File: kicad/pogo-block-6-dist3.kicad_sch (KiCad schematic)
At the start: 62 parts, among them U33 CD4053, U38 TL072, U39 TL072, U44 TL072, U45 TL072, U77 CD4053

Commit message: 0018: block-6 stage 2 - distortion BEFORE bandpass (0017 reorder)
The core 0017 change: flip the per-band order from SVF->DIST to DIST->SVF to
match the plugin (Pogo.cpp:443-451). Realized as a net re-point across the 7
split sections (no part changes):
  LP1_OUT / BP3IN  ->  distN (R18/R20/R22 distortion inputs)
                   ->  mux out (BPn_DISTOUT)  ->  svfN SUM_AMP (R13)
                   ->  SVF v1 buffer (BPn_BANDOUT / BP3_TAP)  ->  mix wet summer
- BP1/BP2 take the LP1 band; BP3 takes BP3IN (the ALT/LP1 selector, stage 3).
- BP3 OUT tap now taken post-bandpass (BP3_TAP = svf3 v1), matching the plugin
  (prevOut[2]); block-B keeps the BP3_TAP net name (no block-B change).
- spec §1/§2 updated: signal order, DIST knob, ALT path (through-VCA/BP3-only),
  BP3 tap point.

Boundary symmetry verified for all re-pointed nets; all 5 --check gates +
parity green.

https://claude.ai/code/session_013jFXG5oeMVSYP7iRpwGvtQ
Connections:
- net BP3_BPBUF_L renamed BP3IN_L
- net BP3_BPBUF_R renamed BP3IN_R
- net BP3_TAP_L renamed BP3_DISTOUT_L
- net BP3_TAP_R renamed BP3_DISTOUT_R
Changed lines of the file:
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@@
   (effects (font (size 1.016 1.016)) (justify left))
 )
-(global_label "BP3_BPBUF_L"
+(global_label "BP3IN_L"
   (shape output)
   (at 40.000 373.810 0)
   (effects (font (size 1.016 1.016)) (justify left))
 )
-(global_label "BP3_BPBUF_L"
+(global_label "BP3IN_L"
   (shape output)
   (at 160.000 373.810 0)
   (effects (font (size 1.016 1.016)) (justify left))
 )
-(global_label "BP3_BPBUF_L"
+(global_label "BP3IN_L"
   (shape output)
   (at 100.000 428.810 0)
   (effects (font (size 1.016 1.016)) (justify left))
 )
-(global_label "BP3_BPBUF_L"
+(global_label "BP3IN_L"
   (shape output)
   (at 40.000 538.810 0)
   (effects (font (size 1.016 1.016)) (justify left))
 )
-(global_label "BP3_BPBUF_L"
+(global_label "BP3IN_L"
   (shape output)
   (at 100.000 538.810 0)
   (effects (font (size 1.016 1.016)) (justify left))
 )
-(global_label "BP3_BPBUF_R"
+(global_label "BP3IN_R"
   (shape output)
   (at 40.000 758.810 0)
   (effects (font (size 1.016 1.016)) (justify left))
 )
-(global_label "BP3_BPBUF_R"
+(global_label "BP3IN_R"
   (shape output)
   (at 160.000 758.810 0)
   (effects (font (size 1.016 1.016)) (justify left))
 )
-(global_label "BP3_BPBUF_R"
+(global_label "BP3IN_R"
   (shape output)
   (at 100.000 813.810 0)
   (effects (font (size 1.016 1.016)) (justify left))
 )
-(global_label "BP3_BPBUF_R"
+(global_label "BP3IN_R"
   (shape output)
   (at 40.000 923.810 0)
   (effects (font (size 1.016 1.016)) (justify left))
 )
-(global_label "BP3_BPBUF_R"
+(global_label "BP3IN_R"
   (shape output)
   (at 100.000 923.810 0)
@@
   (effects (font (size 1.016 1.016)) (justify left))
 )
-(global_label "BP3_TAP_L"
+(global_label "BP3_DISTOUT_L"
   (shape output)
   (at 48.890 50.160 0)
   (effects (font (size 1.016 1.016)) (justify left))
 )
-(global_label "BP3_TAP_R"
+(global_label "BP3_DISTOUT_R"
   (shape output)
   (at 48.890 42.540 0)

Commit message: 0018: block-6 stage 3 - BP3 input selector (ALT-VCA vs LP1)
Build the BP3 input selector the plugin requires (Pogo.cpp:440-441): a CD4053
mux (U81, block-6-dist3) picks per channel between the LP1 band (LP1_OUT) and
the ALT-VCA voice (block-4 ALT_VCA_OUT), feeding BP3's distortion input.
- Select = ALT_L_DET, an ALT_BP_L insertion detect: J3 tip-switch lug (block-1)
  -> ALT_L_DET, +12V pull-up (R133, dist3) + 22k tip pulldown (R134, block-1);
  patched=ALT-VCA, unpatched=LP1.
- BP3IN is now an internal dist3 net (mux out -> distortion), resolving the
  previously hand-waved boundary. New boundary nets: ALT_L_DET (block-1->dist3),
  ALT_VCA_OUT_L/R (block-4->dist3), LP1_OUT extended to dist3.
- Single ALT_L_DET drives both channels (user decision): the locked single-switch
  jacks leave no free contact for an ALT_R detect (J4's switch is the R-normal),
  so the plugin's asymmetric bp3InR=(L||R) is dropped -- diverges only in the
  rare R-patched-not-L case.

CD4053 selector + components (G5/G6a). All 5 --check gates + parity green;
boundary symmetry verified.

https://claude.ai/code/session_013jFXG5oeMVSYP7iRpwGvtQ
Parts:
- added C110_U81n, C110_U81p: 100nF, symbol Device:C
- added R133: 100k, symbol Device:R
- added U81: CD4053, POGO_Package_SO:SOIC-16_3.9x9.9mm_P1.27mm, symbol Analog_Switch:CD4053
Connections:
- net +12V: now also C110_U81p.2, R133.2, U81.9 (C)
- net -12V: now also C110_U81n.2, U81.11 (A)
- net BP3IN_L: now also U81.5 (Z0)
- net BP3IN_R: now also U81.2 (Y0)
- net GND: now also C110_U81n.1, C110_U81p.1, U81.10 (B), U81.12 (X0), U81.13 (X1), U81.14 (X), U81.16 (VDD), U81.6 (INH)
- new net ALT_L_DET: R133.1, U81.7 (VEE), U81.8 (VSS)
- new net ALT_VCA_OUT_L: U81.3 (Z1)
- new net ALT_VCA_OUT_R: U81.1 (Y1)
- new net LP1_OUT_L: U81.4 (Z)
- new net LP1_OUT_R: U81.15 (Y)
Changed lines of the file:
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@@
     (effects (font (size 1.016 1.016)) (justify left) (hide yes)))
 )
+(symbol
+  (lib_id "Analog_Switch:CD4053")
+  (at 160.000 1140.000 0)
+  (unit 1)
+  (in_bom yes)
+  (on_board yes)
+  (property "Reference" "U81" (at 163.000 1143.000 0)
+    (effects (font (size 1.27 1.27)) (justify left)))
+  (property "Value" "CD4053" (at 163.000 1139.500 0)
+    (effects (font (size 1.016 1.016)) (justify left) (hide yes)))
+  (property "Footprint" "POGO_Package_SO:SOIC-16_3.9x9.9mm_P1.27mm" (at 160.000 1140.000 0)
+    (effects (font (size 1.016 1.016)) (hide yes)))
+)
+(symbol
+  (lib_id "Device:C")
+  (at 40.000 1195.000 0)
+  (unit 1)
+  (in_bom yes)
+  (on_board yes)
+  (property "Reference" "C110_U81p" (at 43.000 1198.000 0)
+    (effects (font (size 1.27 1.27)) (justify left)))
+  (property "Value" "100nF" (at 43.000 1194.500 0)
+    (effects (font (size 1.016 1.016)) (justify left) (hide yes)))
+)
+(symbol
+  (lib_id "Device:C")
+  (at 100.000 1195.000 0)
+  (unit 1)
+  (in_bom yes)
+  (on_board yes)
+  (property "Reference" "C110_U81n" (at 103.000 1198.000 0)
+    (effects (font (size 1.27 1.27)) (justify left)))
+  (property "Value" "100nF" (at 103.000 1194.500 0)
+    (effects (font (size 1.016 1.016)) (justify left) (hide yes)))
+)
+(symbol
+  (lib_id "Device:R")
+  (at 160.000 1195.000 0)
+  (unit 1)
+  (in_bom yes)
+  (on_board yes)
+  (property "Reference" "R133" (at 163.000 1198.000 0)
+    (effects (font (size 1.27 1.27)) (justify left)))
+  (property "Value" "100k" (at 163.000 1194.500 0)
+    (effects (font (size 1.016 1.016)) (justify left) (hide yes)))
+)
 (global_label "V5LOGIC"
   (shape output)
@@
 )
 (global_label "BP3IN_L"
-  (shape output)
+  (shape input)
+  (at 168.890 1150.160 0)
+  (effects (font (size 1.016 1.016)) (justify left))
+)
+(global_label "BP3IN_L"
+  (shape input)
   (at 40.000 373.810 0)
   (effects (font (size 1.016 1.016)) (justify left))
 )
 (global_label "BP3IN_L"
-  (shape output)
+  (shape input)
   (at 160.000 373.810 0)
   (effects (font (size 1.016 1.016)) (justify left))
 )
 (global_label "BP3IN_L"
-  (shape output)
+  (shape input)
   (at 100.000 428.810 0)
   (effects (font (size 1.016 1.016)) (justify left))
 )
 (global_label "BP3IN_L"
-  (shape output)
+  (shape input)
   (at 40.000 538.810 0)
   (effects (font (size 1.016 1.016)) (justify left))
 )
 (global_label "BP3IN_L"
-  (shape output)
+  (shape input)
   (at 100.000 538.810 0)
   (effects (font (size 1.016 1.016)) (justify left))
 )
 (global_label "BP3IN_R"
-  (shape output)
+  (shape input)
+  (at 168.890 1142.540 0)
+  (effects (font (size 1.016 1.016)) (justify left))
+)
+(global_label "BP3IN_R"
+  (shape input)
   (at 40.000 758.810 0)
   (effects (font (size 1.016 1.016)) (justify left))
 )
 (global_label "BP3IN_R"
-  (shape output)
+  (shape input)
   (at 160.000 758.810 0)
   (effects (font (size 1.016 1.016)) (justify left))
 )
 (global_label "BP3IN_R"
-  (shape output)
+  (shape input)
   (at 100.000 813.810 0)
   (effects (font (size 1.016 1.016)) (justify left))
 )
 (global_label "BP3IN_R"
-  (shape output)
+  (shape input)
   (at 40.000 923.810 0)
   (effects (font (size 1.016 1.016)) (justify left))
 )
 (global_label "BP3IN_R"
-  (shape output)
+  (shape input)
   (at 100.000 923.810 0)
   (effects (font (size 1.016 1.016)) (justify left))
 )
+(global_label "LP1_OUT_L"
+  (shape output)
+  (at 168.890 1145.080 0)
+  (effects (font (size 1.016 1.016)) (justify left))
+)
+(global_label "LP1_OUT_R"
+  (shape output)
+  (at 168.890 1137.460 0)
+  (effects (font (size 1.016 1.016)) (justify left))
+)
+(global_label "ALT_VCA_OUT_L"
+  (shape output)
+  (at 168.890 1147.620 0)
+  (effects (font (size 1.016 1.016)) (justify left))
+)
+(global_label "ALT_VCA_OUT_R"
+  (shape output)
+  (at 168.890 1140.000 0)
+  (effects (font (size 1.016 1.016)) (justify left))
+)
+(global_label "ALT_L_DET"
+  (shape output)
+  (at 151.110 1147.620 0)
+  (effects (font (size 1.016 1.016)) (justify left))
+)
+(global_label "ALT_L_DET"
+  (shape output)
+  (at 151.110 1145.080 0)
+  (effects (font (size 1.016 1.016)) (justify left))
+)
+(global_label "ALT_L_DET"
+  (shape output)
+  (at 160.000 1191.190 0)
+  (effects (font (size 1.016 1.016)) (justify left))
+)
 (global_label "BP3_SCVG_L"
   (shape input)
@@
   (effects (font (size 1.016 1.016)) (justify left))
 )
+(global_label "+12V"
+  (shape input)
+  (at 151.110 1137.460 0)
+  (effects (font (size 1.016 1.016)) (justify left))
+)
+(global_label "+12V"
+  (shape input)
+  (at 40.000 1198.810 0)
+  (effects (font (size 1.016 1.016)) (justify left))
+)
+(global_label "+12V"
+  (shape input)
+  (at 160.000 1198.810 0)
+  (effects (font (size 1.016 1.016)) (justify left))
+)
 (global_label "-12V"
   (shape input)
@@
   (effects (font (size 1.016 1.016)) (justify left))
 )
+(global_label "-12V"
+  (shape input)
+  (at 151.110 1132.380 0)
+  (effects (font (size 1.016 1.016)) (justify left))
+)
+(global_label "-12V"
+  (shape input)
+  (at 100.000 1198.810 0)
+  (effects (font (size 1.016 1.016)) (justify left))
+)
 (global_label "GND"
   (shape input)
@@
   (effects (font (size 1.016 1.016)) (justify left))
 )
+(global_label "GND"
+  (shape input)
+  (at 151.110 1134.920 0)
+  (effects (font (size 1.016 1.016)) (justify left))
+)
+(global_label "GND"
+  (shape input)
+  (at 151.110 1140.000 0)
+  (effects (font (size 1.016 1.016)) (justify left))
+)
+(global_label "GND"
+  (shape input)
+  (at 168.890 1129.840 0)
+  (effects (font (size 1.016 1.016)) (justify left))
+)
+(global_label "GND"
+  (shape input)
+  (at 168.890 1132.380 0)
+  (effects (font (size 1.016 1.016)) (justify left))
+)
+(global_label "GND"
+  (shape input)
+  (at 168.890 1134.920 0)
+  (effects (font (size 1.016 1.016)) (justify left))
+)
+(global_label "GND"
+  (shape input)
+  (at 151.110 1142.540 0)
+  (effects (font (size 1.016 1.016)) (justify left))
+)
+(global_label "GND"
+  (shape input)
+  (at 40.000 1191.190 0)
+  (effects (font (size 1.016 1.016)) (justify left))
+)
+(global_label "GND"
+  (shape input)
+  (at 100.000 1191.190 0)
+  (effects (font (size 1.016 1.016)) (justify left))
+)

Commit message: 0018: block-6 stage 5 - variable DRIVE (THAT2180 VCA per band)
Build the per-band variable-drive stage the plugin needs (driveCv into the
waveshaper). A stereo THAT2180 current-in/I-V-out VCA per band, inserted at the
distortion input, mirroring the proven block-4 cell pin-for-pin:
  band -> R_in(20k) -> THAT2180.1 ; .8 -> TL074 I/V(-) + R_f(20k) -> BPn_DRIVEOUT
  -> SC/HC/WF cells.  Ec+ (pin2) via Bourns unity trim <- V_DRIVE_CTRL.
Drive control: per-band DRIVE knob (RV33/36/39) + DRIVE CV (MOD_BPn_DIST from
block-3) summed (TL074 half) into Ec+; knob=0.20 ~= unity. A single dB-law VGA
per band approximates the plugin's per-mode gain (SC exp vs HC/WF linear) -- a
documented deviation; exact knob->Ec+ dB law + unity bias are Phase-3R (like
block-4's Ec+ scaling).

Parts: +6 THAT2180 (U85-90), +3 TL074 (U91-93 I/V+summer), +6 Ec+ trims
(RV51-56), R153-176, decoupling. New boundary MOD_BPn_DIST; BPn_DRIVEOUT
internal. RV33/36/39 reused.

NOTE: the I/V stage inverts (as in block-4) -> one inversion added to the BP
wet path; reconcile in the S7 mix polarity-restore so wet sums with dry.

(An initial LM13700-OTA-VGA attempt was rolled back: its input wasn't scaled to
the OTA linear range -- would saturate on +-5V audio. Rebuilt on THAT2180 per
user.) All 5 --check gates + parity green; wiring reviewed vs block-4 template.

https://claude.ai/code/session_013jFXG5oeMVSYP7iRpwGvtQ
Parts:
- added C110_U89n, C110_U89p, C110_U90n, C110_U90p, C110_U93n, C110_U93p: 100nF, symbol Device:C
- added R169, R170, R171, R172: 20k, symbol Device:R
- added R173, R174, R175, R176: 100k, symbol Device:R
- added RV39: BP3_DIST, POGO_Potentiometer_THT:Potentiometer_Alpha_RD901F-40-00D_Single_Vertical_CircularHoles, symbol Device:R_POT
- added RV55: BP3_DRIVE_UNITY_L, POGO_Potentiometer_SMD:Potentiometer_Bourns_3224W, symbol Device:R_POT
- added RV56: BP3_DRIVE_UNITY_R, POGO_Potentiometer_SMD:Potentiometer_Bourns_3224W, symbol Device:R_POT
- added U89, U90: THAT2180, POGO_Package_SIP:SIP-8_2.54mm, symbol POGO:THAT2180
- added U93: TL074, symbol Amplifier_Operational:TL074
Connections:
- net +12V: now also C110_U89p.2, C110_U90p.2, C110_U93p.2, U89.5 (V-), U90.5 (V-), U93.11 (V-)
- net -12V: now also C110_U89n.2, C110_U90n.2, C110_U93n.2, U89.7 (V+), U90.7 (V+), U93.4 (V+)
- net BP3IN_L: now also R169.2; no longer C_WF_3La.2, C_WF_3Lb.2, R18_3L.2, R20_3L.2, R22_3L.2
- net BP3IN_R: now also R170.2; no longer C_WF_3Ra.2, C_WF_3Rb.2, R18_3R.2, R20_3R.2, R22_3R.2
- net GND: now also C110_U89n.1, C110_U89p.1, C110_U90n.1, C110_U90p.1, C110_U93n.1, C110_U93p.1, RV39.3, U89.1 (Input), U89.2 (Ec+), U89.3 (Ec-), U90.1 (Input), U90.2 (Ec+), U90.3 (Ec-), U93.13 (In-), U93.2 (In-), U93.6 (In-), U93.9 (In-)
- net V5LOGIC: now also R175.2, RV39.1
- new net BP3_DRIVEIN_L: R169.1, U89.6 (Gnd)
- new net BP3_DRIVEIN_R: R170.1, U90.6 (Gnd)
- new net BP3_DRIVEIV_L: R171.2, U93.3 (In+)
- new net BP3_DRIVEIV_R: R172.2, U93.5 (In+)
- new net BP3_DRIVEOUT_L: C_WF_3La.2, C_WF_3Lb.2, R171.1, R18_3L.2, R20_3L.2, R22_3L.2, U93.1 (Out)
- new net BP3_DRIVEOUT_R: C_WF_3Ra.2, C_WF_3Rb.2, R172.1, R18_3R.2, R20_3R.2, R22_3R.2, U93.7 (Out)
- new net BP3_DRIVE_KNOB: R173.2, RV39.2 (Wiper)
- new net BP3_DRIVE_SPARE: U93.12 (In+), U93.14 (Out)
- new net BP3_DRIVE_SUM: R173.1, R174.1, R175.1, R176.2, U93.10 (In+)
- new net EC_BP3_DRIVE_L: RV55.2 (Wiper), RV55.3, U89.4 (Sym)
- new net EC_BP3_DRIVE_R: RV56.2 (Wiper), RV56.3, U90.4 (Sym)
- new net MOD_BP3_DIST: R174.2
- new net V_DRIVE_CTRL_3: R176.1, RV55.1, RV56.1, U93.8 (Out)

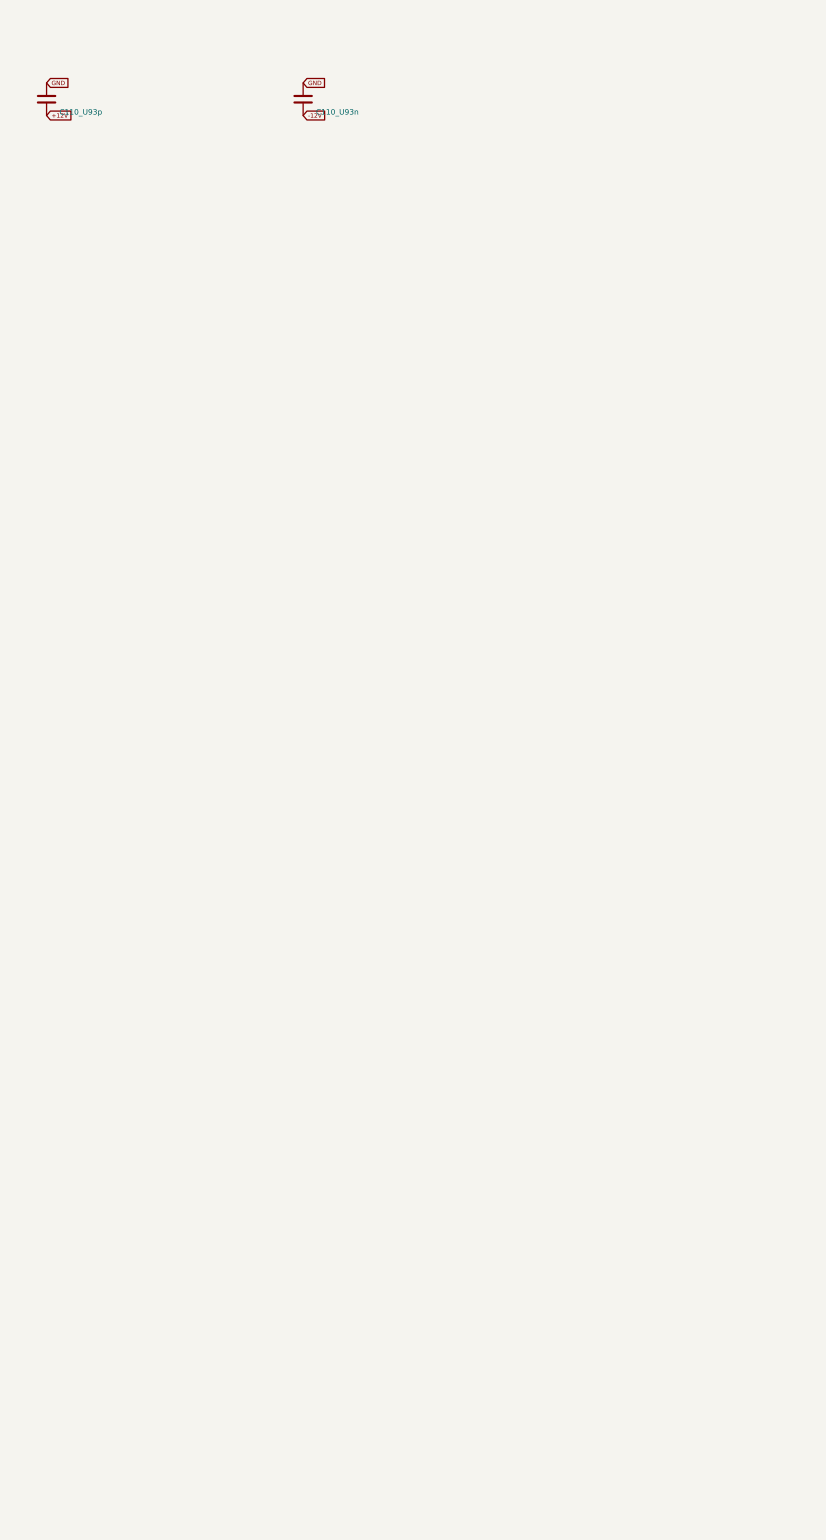
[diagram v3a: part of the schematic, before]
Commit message: 0018: block-6 stage 6 - per-band CLIP LED drivers
The plugin lights BPn_CLIP when max(|distOut_L|,|distOut_R|) > 4V; the panel
has the CLIP LEDs but no hardware drove them. Build a per-band window
detector on the distortion output (BPn_DISTOUT_L/R, the CD4053 mux output):
- TL074 (U94/U95/U96) as 4 comparators per band: DISTOUT_L>+4, <-4,
  DISTOUT_R>+4, <-4, with ~2.2M hysteresis. Outputs diode-OR (D14_*) into
  the panel CLIP LED via a current-limit R.
- Shared +/-4V threshold from a 20k/10k divider off +/-12 (dist1), exported
  as VREF_P4/VREF_N4 boundary nets to dist2/dist3.
- CLIP LED component rows added for BP1/2/3.

All 5 --check gates + parity green. Exact threshold trim is Phase-3R.

https://claude.ai/code/session_013jFXG5oeMVSYP7iRpwGvtQ
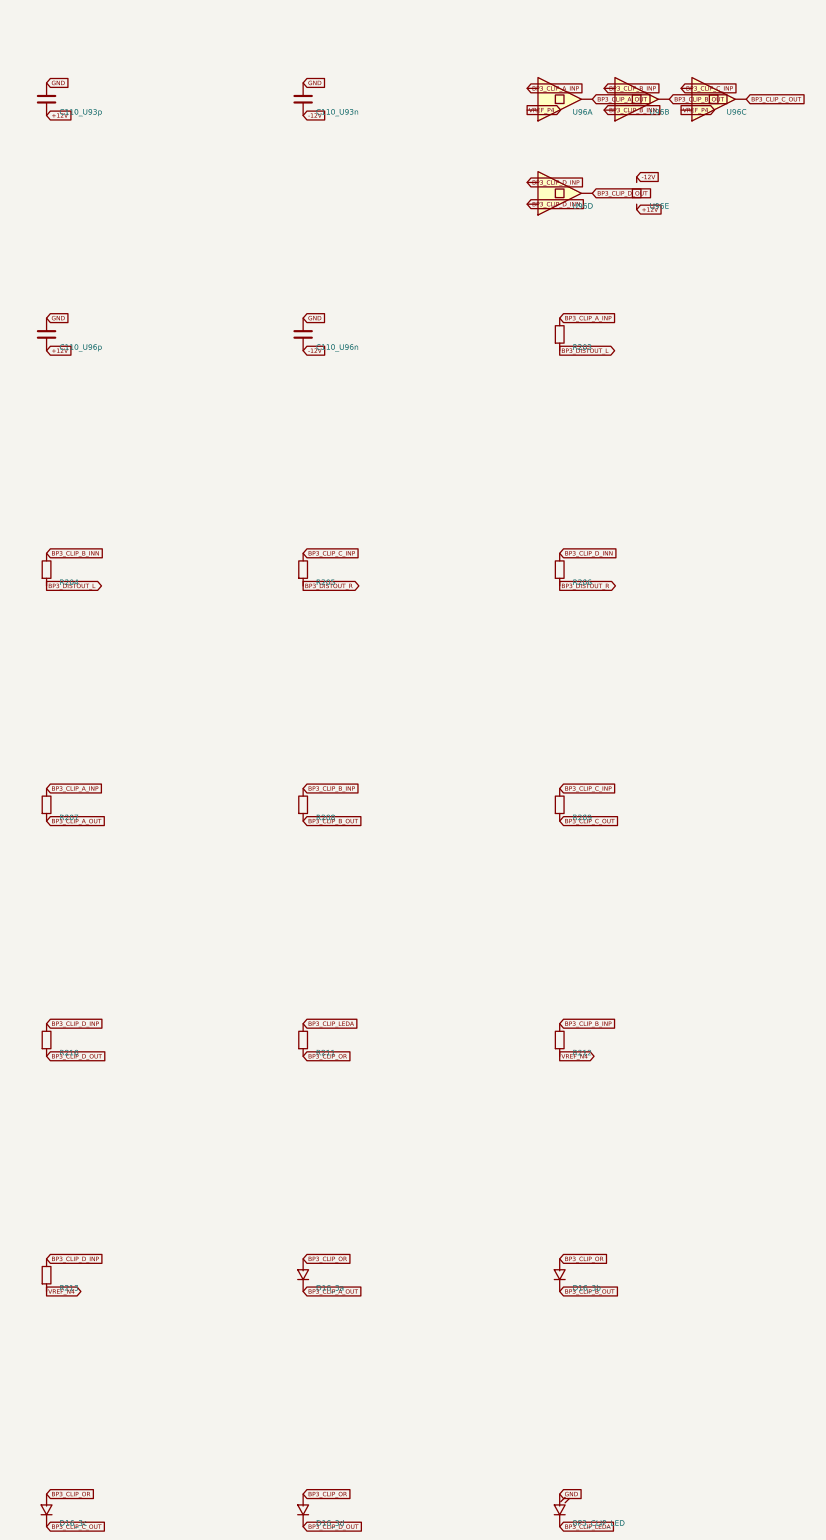
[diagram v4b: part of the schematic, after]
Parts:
- added BP3_CLIP_LED: BP3_CLIP, POGO_LED_THT:LED_D3.0mm, symbol Device:LED
- added C110_U96n, C110_U96p: 100nF, symbol Device:C
- added D16_3a, D16_3b, D16_3c, D16_3d: 1N4148W, POGO_Diode_SMD:D_SOD-123, symbol Device:D
- added R203, R204, R205, R206, R212, R213: 100k, symbol Device:R
- added R207, R208, R209, R210: 2.2M, symbol Device:R
- added R211: 1k, symbol Device:R
- added U96: TL074, POGO_Package_SO:SOIC-14_3.9x8.7mm_P1.27mm, symbol Amplifier_Operational:TL074
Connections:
- net +12V: now also C110_U96p.2, U96.11 (V-)
- net -12V: now also C110_U96n.2, U96.4 (V+)
- net BP3_DISTOUT_L: now also R203.2, R204.2
- net BP3_DISTOUT_R: now also R205.2, R206.2
- net GND: now also BP3_CLIP_LED.A, C110_U96n.1, C110_U96p.1
- new net BP3_CLIP_A_INP: R203.1, R207.1, U96.2 (In-)
- new net BP3_CLIP_A_OUT: D16_3a.K, R207.2, U96.1 (Out)
- new net BP3_CLIP_B_INN: R204.1, U96.5 (In+)
- new net BP3_CLIP_B_INP: R208.1, R212.1, U96.6 (In-)
- new net BP3_CLIP_B_OUT: D16_3b.K, R208.2, U96.7 (Out)
- new net BP3_CLIP_C_INP: R205.1, R209.1, U96.9 (In-)
- new net BP3_CLIP_C_OUT: D16_3c.K, R209.2, U96.8 (Out)
- new net BP3_CLIP_D_INN: R206.1, U96.12 (In+)
- new net BP3_CLIP_D_INP: R210.1, R213.1, U96.13 (In-)
- new net BP3_CLIP_D_OUT: D16_3d.K, R210.2, U96.14 (Out)
- new net BP3_CLIP_LEDA: BP3_CLIP_LED.K, R211.1
- new net BP3_CLIP_OR: D16_3a.A, D16_3b.A, D16_3c.A, D16_3d.A, R211.2
- new net VREF_N4: R212.2, R213.2
- new net VREF_P4: U96.10 (In+), U96.3 (In+)
